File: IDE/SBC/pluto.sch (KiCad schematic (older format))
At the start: 3 parts, among them U1 WD65C02_, U2 WD65C22

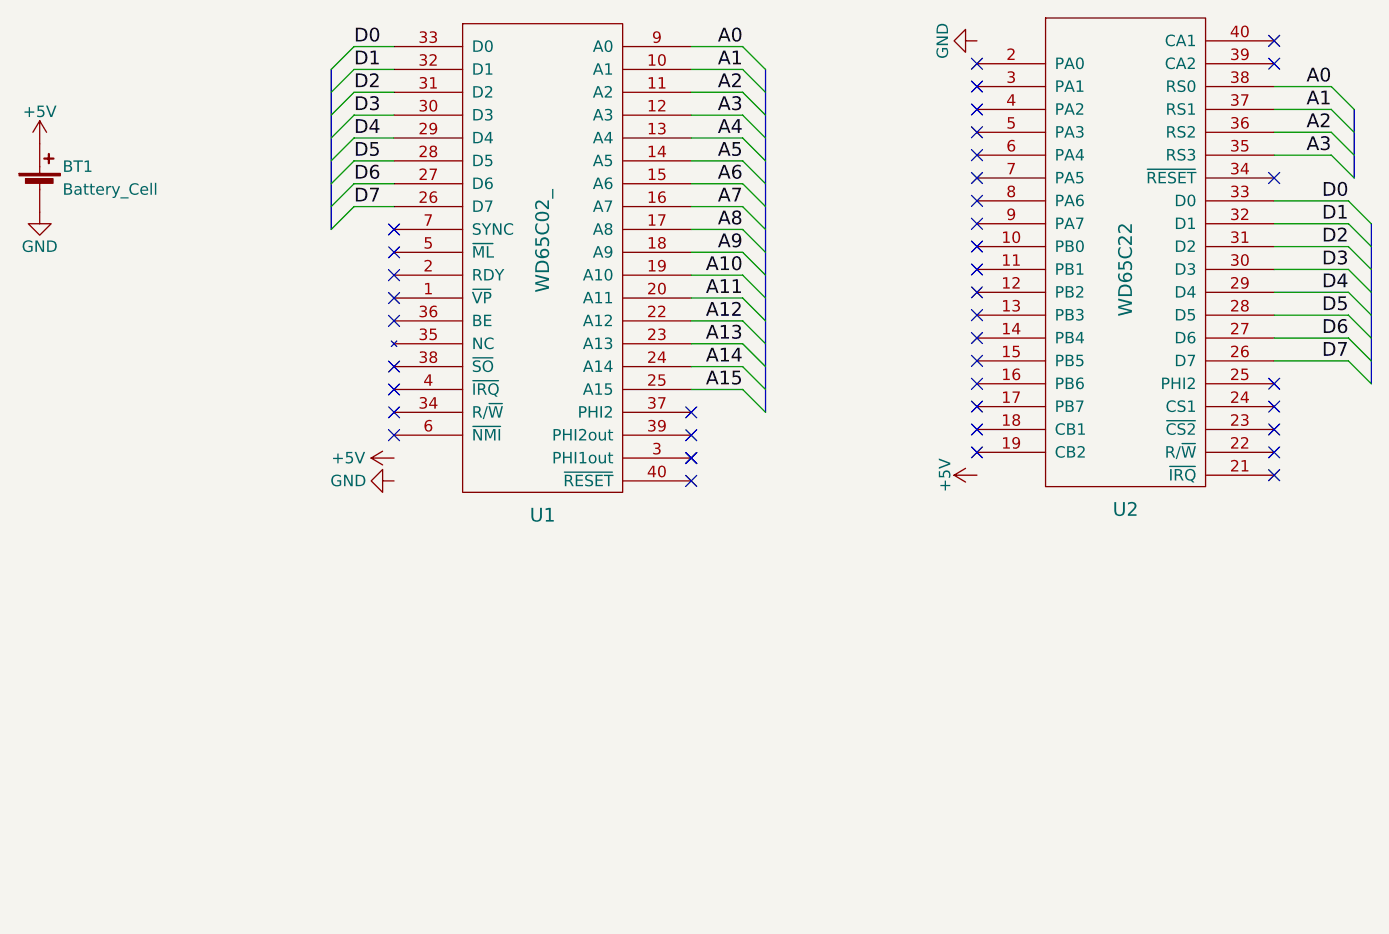
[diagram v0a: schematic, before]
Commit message: Changed names of IO select lines.
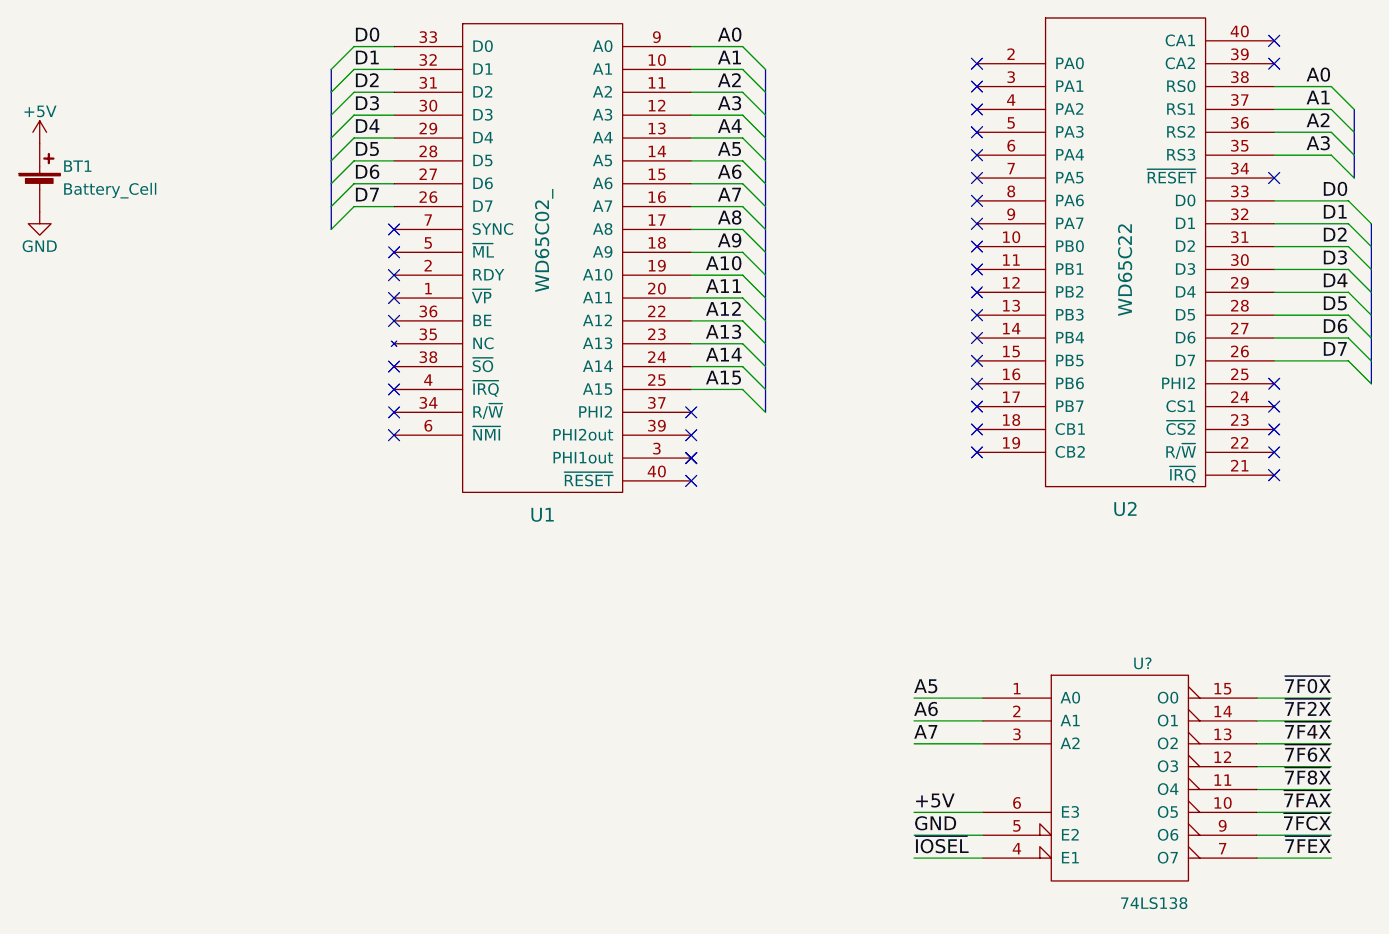
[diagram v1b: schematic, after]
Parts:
- added U?: 74LS138, symbol 74LS138
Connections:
- net +5V: now also U?.6 (E3); no longer U1.8 (VCC), U2.20 (VCC)
- net A5: now also U?.1 (A0)
- net A6: now also U?.2 (A1)
- net A7: now also U?.3 (A2)
- net GND: now also U?.5 (E2), U?.8 (GND); no longer U2.1 (GND)
- new net VCC: U1.8 (VCC), U2.20 (VCC), U?.16 (VCC)
- new net ~7F0X: U?.15 (O0)
- new net ~7F2X: U?.14 (O1)
- new net ~7F4X: U?.13 (O2)
- new net ~7F6X: U?.12 (O3)
- new net ~7F8X: U?.11 (O4)
- new net ~7FAX: U?.10 (O5)
- new net ~7FCX: U?.9 (O6)
- new net ~7FEX: U?.7 (O7)
- new net ~IOSEL: U?.4 (E1)
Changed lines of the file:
@@
 NoConn ~ 6275 3775
 NoConn ~ 6275 3875
-$Comp
-L GND #PWR01
-U 1 1 58D16CA0
-P 4975 1975
-F 0 "#PWR01" H 4975 1725 50  0001 C CNN
-F 1 "GND" H 4975 1825 50  0000 C CNN
-F 2 "" H 4975 1975 50  0001 C CNN
-F 3 "" H 4975 1975 50  0001 C CNN
-	1    4975 1975
-	0    1    1    0
-$EndComp
-$Comp
-L +5V #PWR02
-U 1 1 58D16CC2
-P 4975 3875
-F 0 "#PWR02" H 4975 3725 50  0001 C CNN
-F 1 "+5V" H 4975 4015 50  0000 C CNN
-F 2 "" H 4975 3875 50  0001 C CNN
-F 3 "" H 4975 3875 50  0001 C CNN
-	1    4975 3875
-	0    -1   -1   0
-$EndComp
-$Comp
-L +5V #PWR03
-U 1 1 58D16CF8
-P 2425 3800
-F 0 "#PWR03" H 2425 3650 50  0001 C CNN
-F 1 "+5V" V 2425 4000 50  0000 C CNN
-F 2 "" H 2425 3800 50  0001 C CNN
-F 3 "" H 2425 3800 50  0001 C CNN
-	1    2425 3800
-	0    -1   -1   0
-$EndComp
-$Comp
-L GND #PWR04
-U 1 1 58D16D3A
-P 2425 3900
-F 0 "#PWR04" H 2425 3650 50  0001 C CNN
-F 1 "GND" V 2425 3700 50  0000 C CNN
-F 2 "" H 2425 3900 50  0001 C CNN
-F 3 "" H 2425 3900 50  0001 C CNN
-	1    2425 3900
-	0    1    1    0
-$EndComp
 NoConn ~ 3725 3600
 NoConn ~ 3725 3700
@@
 Wire Bus Line
 	6625 2275 6625 2575
+$Comp
+L 74LS138 U?
+U 1 1 58D4412E
+P 5600 5200
+F 0 "U?" H 5700 5700 50  0000 C CNN
+F 1 "74LS138" H 5750 4651 50  0000 C CNN
+F 2 "" H 5600 5200 50  0001 C CNN
+F 3 "" H 5600 5200 50  0001 C CNN
+	1    5600 5200
+	1    0    0    -1
+$EndComp
+Wire Wire Line
+	5000 4850 4700 4850
+Wire Wire Line
+	5000 4950 4700 4950
+Wire Wire Line
+	5000 5050 4700 5050
+Wire Wire Line
+	5000 5350 4700 5350
+Wire Wire Line
+	5000 5450 4700 5450
+Wire Wire Line
+	5000 5550 4700 5550
+Text Label 4700 4850 0    60   ~ 0
+A5
+Text Label 4700 4950 0    60   ~ 0
+A6
+Text Label 4700 5050 0    60   ~ 0
+A7
+Text Label 4700 5550 0    60   ~ 0
+~IOSEL
+Wire Wire Line
+	6200 4850 6525 4850
+Wire Wire Line
+	6200 4950 6525 4950
+Wire Wire Line
+	6200 5050 6525 5050
+Wire Wire Line
+	6200 5150 6525 5150
+Wire Wire Line
+	6200 5250 6525 5250
+Wire Wire Line
+	6200 5350 6525 5350
+Wire Wire Line
+	6200 5450 6525 5450
+Wire Wire Line
+	6200 5550 6525 5550
+Text Label 6525 4850 2    60   ~ 0
+~7F0X
+Text Label 6525 4950 2    60   ~ 0
+~7F2X
+Text Label 6525 5050 2    60   ~ 0
+~7F4X
+Text Label 6525 5150 2    60   ~ 0
+~7F6X
+Text Label 6525 5250 2    60   ~ 0
+~7F8X
+Text Label 6525 5350 2    60   ~ 0
+~7FAX
+Text Label 6525 5450 2    60   ~ 0
+~7FCX
+Text Label 6525 5550 2    60   ~ 0
+~7FEX
+Text Label 4700 5350 0    60   ~ 0
++5V
+Text Label 4700 5450 0    60   ~ 0
+GND
 $EndSCHEMATC
